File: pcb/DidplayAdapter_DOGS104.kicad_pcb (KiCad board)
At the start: 2 copper layers, 39 x 30 mm, 13 parts, among them J1 EA_DOGS104, J2 Amber, U1 EA_DOGS104x-A

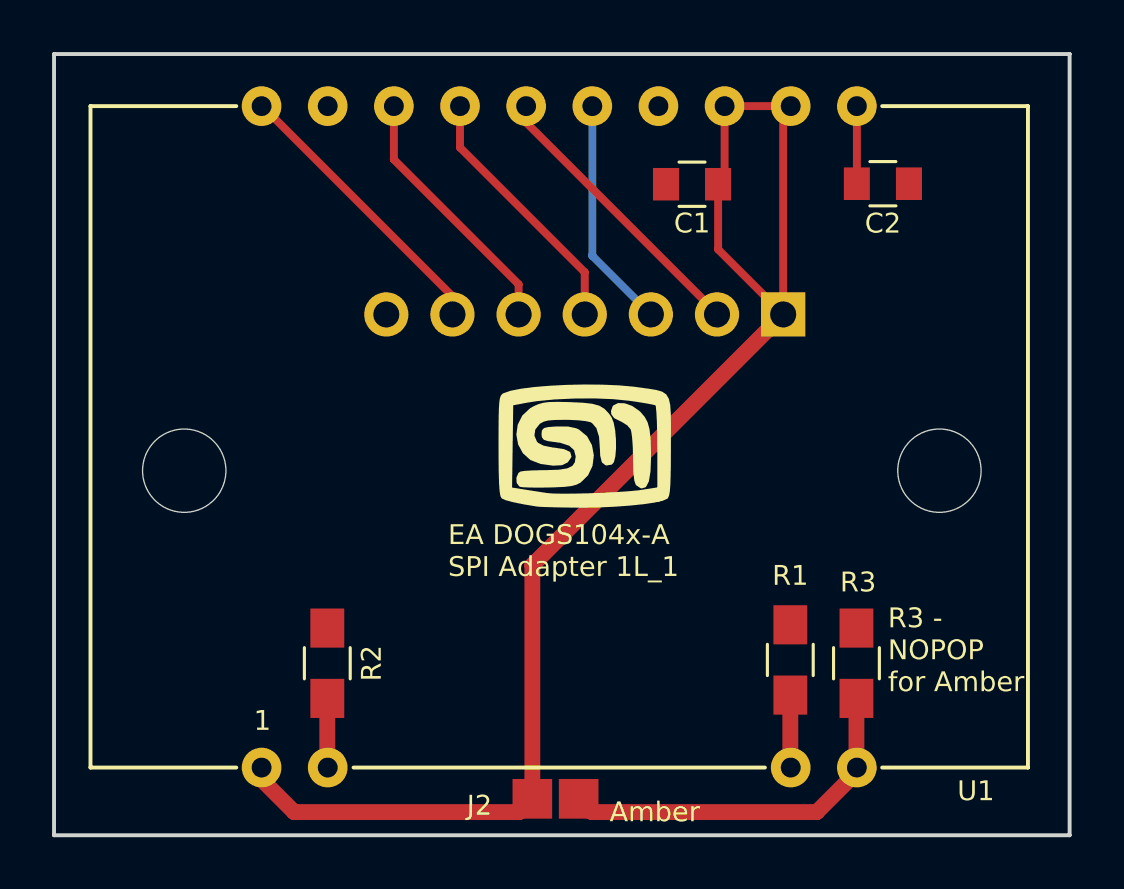
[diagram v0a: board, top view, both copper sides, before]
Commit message: Complted the Rev2 layout and sent to OSHPark. Feature for back-light
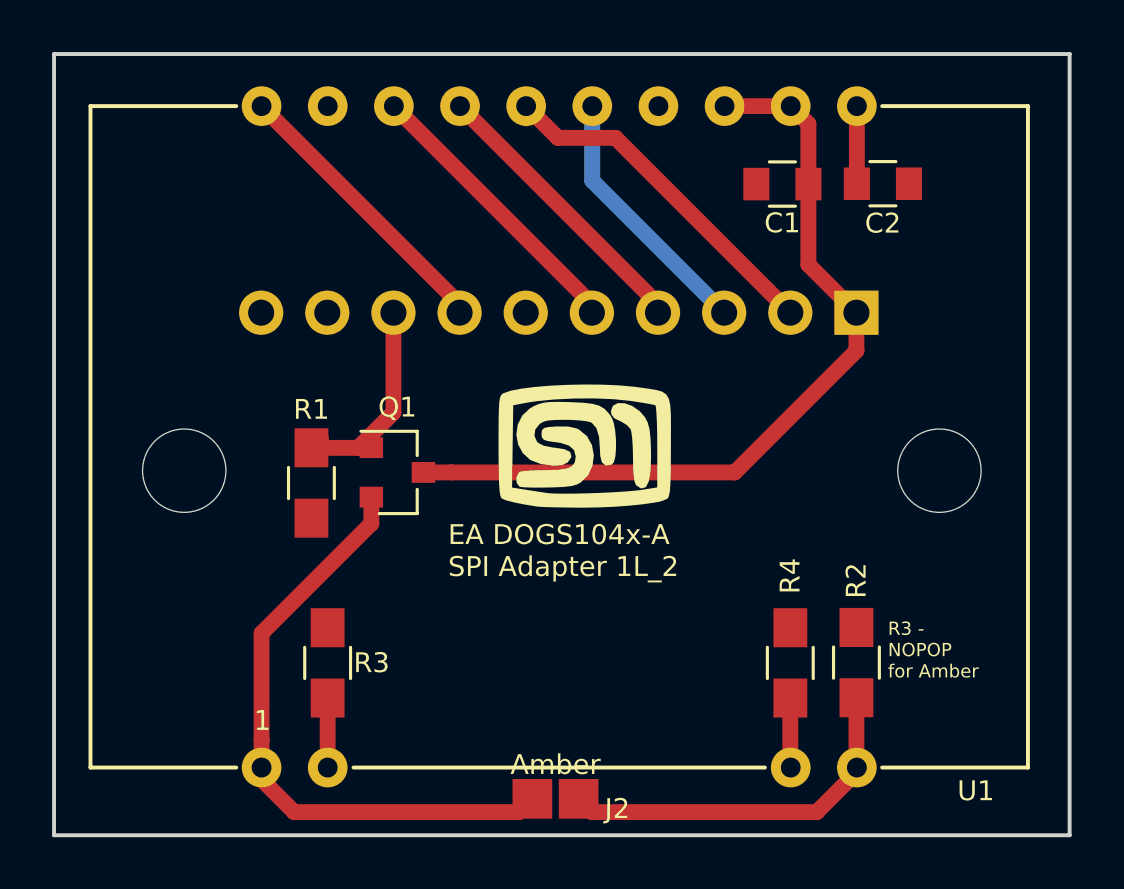
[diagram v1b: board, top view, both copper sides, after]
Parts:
- added Q1: Q_NMOS_GSD, TO_SOT_Packages_SMD:SOT-23, F.Cu at (145.2, 105.1)
- added R4: 7Ω, Resistors_SMD:R_0805_HandSoldering, F.Cu at (160.3, 112.4)
- J1: footprint Pin_Headers:Pin_Header_Straight_1x07_Pitch2.54mm -> Pin_Headers:Pin_Header_Straight_1x10_Pitch2.54mm
- R1: value 7Ω -> 10kΩ
- R2: value 27Ω -> 10Ω
- R3: value 10Ω -> 27Ω
- moved R2 20.3 mm to (162.8, 112.4)
- moved R3 20.3 mm to (142.5, 112.4)
- moved R1 19.6 mm to (141.9, 105.5), turned to 90 degrees
- moved C1 3.47 mm to (160.0, 94.0)
- moved J1 2.81 mm to (162.8, 98.9)
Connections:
- J1 pad 6: /~RESET -> (no net)
- J1 pad 7: GND -> /~RESET
- J2 pad 2: /Vdd -> Net-(J2-Pad2)
- R1 pad 2: Net-(R1-Pad2) -> /BACKLIGHT
- R2 pad 2: Net-(R2-Pad2) -> Net-(J2-Pad1)
- R3 pad 2: Net-(J2-Pad1) -> Net-(R3-Pad2)
- U1 pad 1: /Vdd -> Net-(J2-Pad2)
- U1 pad 2: Net-(R2-Pad2) -> Net-(R3-Pad2)
- U1 pad 9: Net-(R1-Pad2) -> Net-(R4-Pad2)
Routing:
- net Net-(J2-Pad2): track 0.00 -> 23.7 mm
- net /Vdd: track 54.0 -> 32.3 mm
- net /BACKLIGHT: track 0.00 -> 8.63 mm
- net /MOSI: track 11.0 -> 14.1 mm
- net Net-(R1-Pad2): track 2.79 -> 0.00 mm
- net Net-(R4-Pad2): track 0.00 -> 2.67 mm
- net Net-(R3-Pad2): track 0.00 -> 2.67 mm
- net Net-(R2-Pad2): track 2.66 -> 0.00 mm
- net /MISO: track 8.93 -> 10.0 mm
- net /~CS: track 9.98 -> 11.1 mm
- net /CLK: track 9.98 -> 11.1 mm
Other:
- board text added: "EA DOGS104x-A SPI Adapter 1L_2"
- board text added: "GND N/C BK_LT ~RESET N/C ~CS CLK MISO MOSI Vdd"
- board text removed: "EA DOGS104x-A SPI Adapter 1L_1"
- board text removed: "GND ~RESET ~CS CLK MISO MOSI Vdd"
